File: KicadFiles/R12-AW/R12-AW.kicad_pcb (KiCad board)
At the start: 2 copper layers, 226.7 x 75 mm, 126 parts, among them J1 Conn_01x01_Pin, J2 Conn_01x04_MountingPin, J3 Conn_01x04_MountingPin, SW1 SW_DPST_x2, SW2 SW_DPST_x2, U1 TPD4E05U06DQAR, U2 STM32F072CBTx, U3 XC6206PxxxMR

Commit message: Add global labels for columns and rows in R13-AH schematic
- Introduced new global labels for columns (Col0 to Col12) and rows (Row0 to Row3) in the R13-AH schematic.
- Each label includes properties for intersheet references, font size, justification, and positioning.
- Enhanced organization and readability of the schematic by clearly defining input and output connections.
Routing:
- net GND: vias 27 -> 30

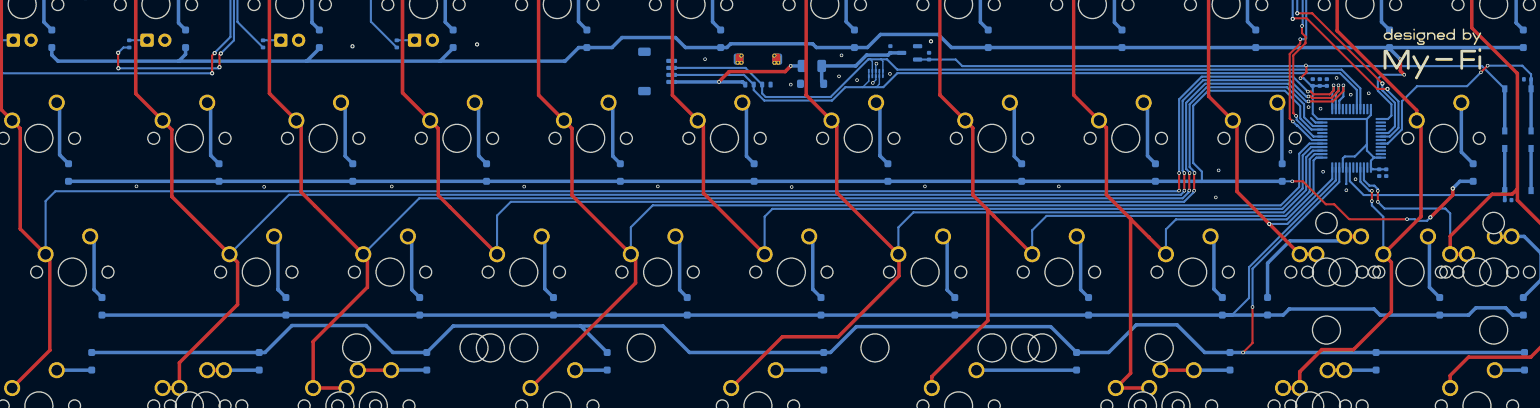
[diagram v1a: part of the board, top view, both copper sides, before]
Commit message: Update DRC exclusions and modify error handling in R13-AH.kicad_pro
- Added multiple DRC exclusions for specific footprints and hole clearances.
- Changed DRC error handling settings for courtyards overlap, hole to hole, nonmirrored text on back layer, silk edge clearance, silk over copper, and silk overlap to "ignore".
- Updated solder mask to copper clearance from 0.0 to 0.005.
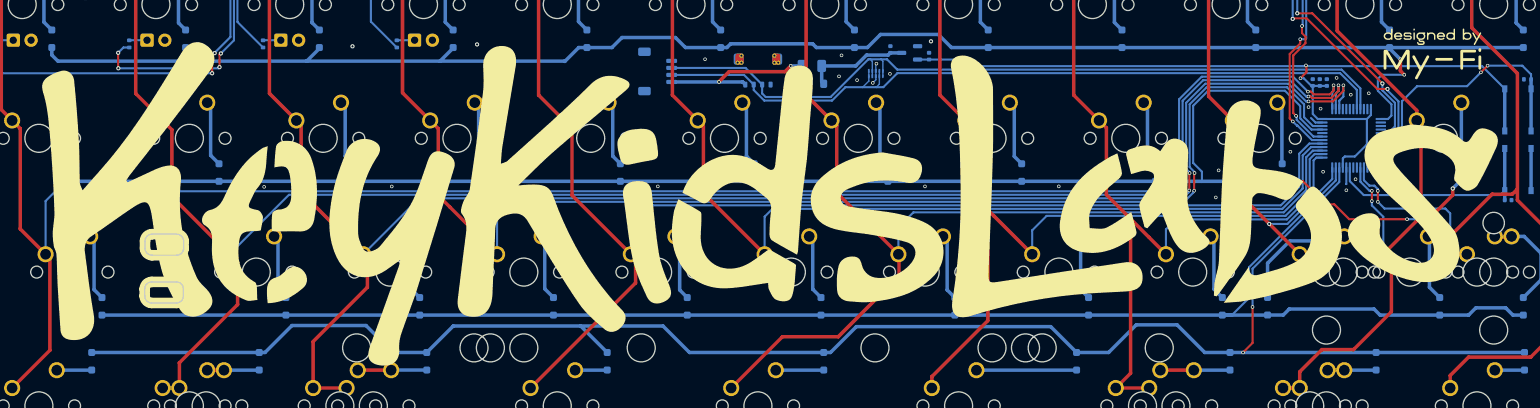
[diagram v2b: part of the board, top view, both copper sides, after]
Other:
- outline, holes or cut-outs redrawn
